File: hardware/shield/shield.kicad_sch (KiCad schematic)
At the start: 15 parts, among them J1 Conn_01x18, J2 Conn_01x20, J3 Conn_01x20, J4 BAT, J5 DCDC, J6 DCDC, U1 NUCLEO-N657X0-Q

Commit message: first schematic version and .ioc pin config
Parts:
- added C10, C11, C12, C14, C15, C16, C17, C18, C19, C20, C21, C22, C23, C24, C25, C28, C29, C6, C7, C8, C9: 0.1uF, Capacitor_SMD:C_0603_1608Metric, symbol Device:C
- added C13: 100uF, Capacitor_Tantalum_SMD:CP_EIA-3528-12_Kemet-T, symbol Device:C_Polarized
- added C26: 1uF, Capacitor_SMD:C_0805_2012Metric, symbol Device:C
- added C27: 47uF, Capacitor_Tantalum_SMD:CP_EIA-3528-12_Kemet-T, symbol Device:C_Polarized
- added J10: Conn_01x09, symbol Connector_Generic:Conn_01x09
- added J11, J12, J24, J25, J27, J28, J29, J30, J31, J7, J8: Conn_01x03, symbol Connector_Generic:Conn_01x03
- added J13, J26, J33: Conn_01x04, symbol Connector_Generic:Conn_01x04
- added J14: DCDC, symbol Connector_Generic:Conn_01x03
- added J15, J16, J17, J18, J19, J20, J21, J22, J23: Conn_01x01_Pin, symbol Connector:Conn_01x01_Pin
- added J32: Conn_01x08, symbol Connector_Generic:Conn_01x08
- added J9: Conn_01x10, symbol Connector_Generic:Conn_01x10
- added R10, R4, R6: 2.2k, symbol Device:R
- added R3, R5: 1.2k, symbol Device:R
- added R7: 10k, symbol Device:R
- added R8: 1k, symbol Device:R
- added R9: 1.5k, symbol Device:R
- added U2: AMS1117-3.3, Package_TO_SOT_SMD:SOT-223-3_TabPin2, symbol Regulator_Linear:AMS1117-3.3
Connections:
- net 3V3: now also C11.1, C15.1, C16.1, C20.1, C21.1, C22.1, C23.1, C26.1, C27.1, C8.1, C9.1, J10.1 (Pin_1), J12.2 (Pin_2), J17.1 (Pin_1), J18.1 (Pin_1), J28.3 (Pin_3), J29.3 (Pin_3), J30.3 (Pin_3), J31.3 (Pin_3), J9.1 (Pin_1), U2.2 (VO); no longer U1.16 (3V3)
- net 5V: now also C10.1, C29.1, J11.2 (Pin_2), J33.4 (Pin_4), U2.3 (VI)
- net 8V: now also C6.1, C7.1, J7.2 (Pin_2), J8.2 (Pin_2)
- net GND: now also C10.2, C11.2, C12.2, C13.2, C14.2, C15.2, C16.2, C17.2, C18.2, C19.2, C20.2, C21.2, C22.2, C23.2, C24.2, C25.2, C26.2, C27.2, C28.2, C29.2, C6.2, C7.2, C8.2, C9.2, J10.2 (Pin_2), J11.1 (Pin_1), J12.1 (Pin_1), J13.1 (Pin_1), J14.3 (Pin_3), J19.1 (Pin_1), J20.1 (Pin_1), J21.1 (Pin_1), J22.1 (Pin_1), J23.1 (Pin_1), J24.1 (Pin_1), J25.1 (Pin_1), J26.1 (Pin_1), J27.1 (Pin_1), J28.1 (Pin_1), J29.1 (Pin_1), J30.1 (Pin_1), J31.1 (Pin_1), J32.1 (Pin_1), J33.1 (Pin_1), J7.1 (Pin_1), J8.1 (Pin_1), J9.2 (Pin_2), R10.2, R4.2, R6.2, R8.1, U2.1 (GND)
- net OV_FLASH: now also U1.64 (PB15); no longer U1.38 (PH2)
- net VCC: now also C24.1, J14.1 (Pin_1), J32.8 (Pin_8), R7.2
- net MOT_PWM1: now reaches U1.40 (NC/PB1)
- net MOT_PWM1: now also J32.7 (Pin_7)
- net IMU_SCK: now reaches U1.42 (PF2)
- net IMU_SCK: now also J9.3 (Pin_3)
- net MOT_BAT: now reaches U1.43 (MOD_PA12)
- net MOT_BAT: now also J32.2 (Pin_2)
- net IR_3: now reaches U1.45 (MOD_PF3)
- net IR_3: now also J30.2 (Pin_2)
- net IR_1: now reaches U1.52 (MOD_PA8)
- net IR_1: now also J28.2 (Pin_2)
- net GEN_TX: now reaches U1.61 (PG3)
- net GEN_TX: now also J24.2 (Pin_2)
- net TEL_TX: now reaches U1.70 (PH3)
- net TEL_TX: now also U1.105 (PD8), J13.2 (Pin_2)
- net TEL_RX: now reaches U1.107 (PD9)
- net TEL_RX: now also J13.3 (Pin_3)
- net BAT_U: now reaches U1.108 (PA1)
- net BAT_U: now also C25.1, R7.1, R8.2
- net UI_SCL: now reaches U1.73 (PH9)
- net UI_SCL: now also J10.7 (Pin_7)
- net UI_SDA: now reaches U1.75 (PC1)
- net UI_SDA: now also J10.8 (Pin_8)
- net SERVO_REAR: now reaches U1.76 (PD6)
- net SERVO_REAR: now also J7.3 (Pin_3)
- net RX_PWM: now reaches U1.83 (PG1)
- net RX_PWM: now also R3.2, R4.1
- net LED_DATA: now reaches U1.85 (PG2)
- net LED_DATA: now also R5.2, R6.1
- net GEN_SCK: now reaches U1.86 (PB9)
- net GEN_SCK: now also J25.3 (Pin_3)
- net GEN_TIM: now reaches U1.93 (PE11)
- net GEN_TIM: now also J26.4 (Pin_4)
- net CMD_RX: now reaches U1.99 (PE0)
- net CMD_RX: now also J12.3 (Pin_3)
- net IMU_MISO: now reaches U1.13 (PC4)
- net IMU_MISO: now also J9.7 (Pin_7)
- net GEN_MOSI: now reaches U1.25 (PC3)
- net GEN_MOSI: now also J25.2 (Pin_2)
- net GEN_RX: now reaches U1.3 (PC2)
- net GEN_RX: now also J24.3 (Pin_3)
- net IR_2: now reaches U1.32 (PF6)
- net IR_2: now also J29.2 (Pin_2)
- net MOT_I: now reaches U1.34 (PA2)
- net MOT_I: now also C28.1, R10.1, R9.2
- net SERVO_FRONT: now reaches U1.36 (PC12)
- net SERVO_FRONT: now also J8.3 (Pin_3)
- net MOT_PWM2: now reaches U1.37 (PC8)
- net MOT_PWM2: now also J32.6 (Pin_6)
- net MOT_STATUS: now reaches U1.110 (PP1)
- net MOT_STATUS: now also J32.4 (Pin_4)
- net MOT_EN: now reaches U1.111 (PP0)
- net MOT_EN: now also J32.5 (Pin_5)
- net UI_BACK: now reaches U1.112 (PP2)
- net UI_BACK: now also J10.3 (Pin_3)
- net UI_A: now reaches U1.114 (PP3)
- net UI_A: now also J10.4 (Pin_4)
- net UI_B: now reaches U1.116 (PP4)
- net UI_B: now also J10.5 (Pin_5)
- net UI_PUSH: now reaches U1.118 (PP5)
- net UI_PUSH: now also J10.6 (Pin_6)
- net UI_CONF: now reaches U1.120 (PP6)
- net UI_CONF: now also J10.9 (Pin_9)
- net GEN_PIN1: now reaches U1.122 (PP7)
- net GEN_PIN1: now also J26.3 (Pin_3)
- net GEN_PIN2: now reaches U1.126 (PP8)
- net GEN_PIN2: now also J26.2 (Pin_2)
- net ENC_A: now reaches U1.127 (PD13)
- net ENC_A: now also J33.2 (Pin_2)
- net IMU_MOSI: now reaches U1.128 (PP9)
- net IMU_MOSI: now also J9.4 (Pin_4)
- net ENC_B: now reaches U1.137 (PG13)
- net ENC_B: now also J33.3 (Pin_3)
- new net: J27.2 (Pin_2), R5.1
- new net: J11.3 (Pin_3), R3.1
- new net: J32.3 (Pin_3), R9.1
- new net 5V_EXT: C12.1, C13.1, C14.1, C17.1, C18.1, C19.1, J13.4 (Pin_4), J14.2 (Pin_2), J15.1 (Pin_1), J16.1 (Pin_1), J27.3 (Pin_3)
- new net IR_4: J31.2 (Pin_2), U1.38 (PH2)
- no-connect marks 23 -> 16
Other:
- note added: "!!!"
- note added: "1V8!!!"
- note added: "Command module"
- note added: "Control"
- note added: "Distance"
- note added: "Extras"
- note added: "Front Servo"
- note added: "IMU"
- note added: "Motor"
- note added: "RC receiver"
- note added: "Rear Servo"
- note added: "Telemetry UART"
- note added: "UI"
- note added: "Using DCDC converter modules like these: https://www.aliexpress.com/item/1005001821783419.html"
- note added: "Using a UI module like this: https://www.hestore.hu/prod_10048024.html#"
- moved on the sheet: C1, C2, C3, C4, C5, F1, J1, J2, J3, J4, J5, J6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

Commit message: minor sch fixes and footprint assignment
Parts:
- removed C1: 220uF, Capacitor_Tantalum_SMD:CP_EIA-3528-12_Kemet-T, symbol Device:C_Polarized
- added C1: 0.1uF, Capacitor_SMD:C_0603_1608Metric, symbol Device:C
- added C30: 1uF, Capacitor_SMD:C_0805_2012Metric, symbol Device:C
- added C31, C32: 220uF, Capacitor_SMD:CP_Elec_6.3x7.7, symbol Device:C_Polarized
- added J34: DCDC, Connector_PinHeader_2.54mm:PinHeader_1x03_P2.54mm_Vertical, symbol Connector_Generic:Conn_01x03
- added J35: Conn_01x03, Connector_PinHeader_1.00mm:PinHeader_1x03_P1.00mm_Vertical, symbol Connector_Generic:Conn_01x03
- added JP1, JP2, JP3: SolderJumper_2_Open, Jumper:SolderJumper-2_P1.3mm_Open_TrianglePad1.0x1.5mm, symbol Jumper:SolderJumper_2_Open
- C13, C2: footprint Capacitor_Tantalum_SMD:CP_EIA-3528-12_Kemet-T -> Capacitor_SMD:CP_Elec_5x5.8
- C27: footprint Capacitor_Tantalum_SMD:CP_EIA-3528-12_Kemet-T -> Capacitor_SMD:CP_Elec_5x5.3
- F1: value 5A -> 8A; footprint Fuse:Fuse_0805_2012Metric -> Fuse:Fuseholder_Blade_Mini_Keystone_3568
- J1: footprint (none) -> Connector_PinHeader_2.00mm:PinHeader_2x09_P2.00mm_Horizontal
- J10: footprint (none) -> Connector_JST:JST_SH_SM09B-SRSS-TB_1x09-1MP_P1.00mm_Horizontal
- J11, J12, J27, J28, J29, J30, J31: footprint (none) -> Connector_JST:JST_SH_SM03B-SRSS-TB_1x03-1MP_P1.00mm_Horizontal
- J13, J33: footprint (none) -> Connector_JST:JST_SH_SM04B-SRSS-TB_1x04-1MP_P1.00mm_Horizontal
- J14, J5, J6: footprint (none) -> Connector_PinHeader_2.54mm:PinHeader_1x03_P2.54mm_Vertical
- J15, J16, J17, J18, J19, J20, J21, J22, J23: footprint (none) -> Connector_Pin:Pin_D0.7mm_L6.5mm_W1.8mm_FlatFork
- J2, J3: footprint (none) -> Connector_PinHeader_2.00mm:PinHeader_2x10_P2.00mm_Horizontal
- J24, J25: footprint (none) -> Connector_PinHeader_1.00mm:PinHeader_1x03_P1.00mm_Vertical
- J26: footprint (none) -> Connector_PinHeader_1.00mm:PinHeader_1x04_P1.00mm_Vertical
- J32: footprint (none) -> Connector_JST:JST_SH_SM08B-SRSS-TB_1x08-1MP_P1.00mm_Horizontal
- J4: footprint (none) -> TerminalBlock:TerminalBlock_MaiXu_MX126-5.0-02P_1x02_P5.00mm
- J7, J8: footprint (none) -> Connector_PinHeader_2.54mm:PinHeader_1x03_P2.54mm_Horizontal
- J9: footprint (none) -> Connector_PinHeader_2.54mm:PinHeader_1x10_P2.54mm_Vertical
- R1, R10, R2, R3, R4, R5, R6, R7, R8, R9: footprint (none) -> Resistor_SMD:R_0603_1608Metric
- U1: footprint FP_NUCLEO-144 - N6 -> hallglib:FP_NUCLEO-144 - N6
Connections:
- net 3V3: now also JP3.1 (A); no longer C20.1, C21.1, C22.1, C23.1, C26.1, C27.1, J28.3 (Pin_3), J29.3 (Pin_3), J30.3 (Pin_3), J31.3 (Pin_3), U2.2 (VO)
- net 5V: now also C30.1, JP1.2 (B); no longer C2.1, C3.1, J5.2 (Pin_2)
- net 5V_EXT: now also C20.1, C21.1, C22.1, C23.1, J28.3 (Pin_3), J29.3 (Pin_3), J30.3 (Pin_3), J31.3 (Pin_3), JP2.2 (B); no longer C12.1, C13.1, J14.2 (Pin_2)
- net GND: now also C1.2, C30.2, C31.2, C32.2, J34.3 (Pin_3), J35.1 (Pin_1)
- net OV_I2C4_SCL: now also J35.2 (Pin_2)
- net OV_I2C4_SDA: now also J35.3 (Pin_3)
- net 8V renamed 8V_1
- net 8V_1: now also C32.1; no longer C7.1, J7.2 (Pin_2)
- net VCC renamed VBAT
- net VBAT: now also J34.1 (Pin_1)
- new net: C12.1, C13.1, J14.2 (Pin_2), JP2.1 (A)
- new net: C2.1, C3.1, J5.2 (Pin_2), JP1.1 (A)
- new net: C26.1, C27.1, JP3.2 (B), U2.2 (VO)
- new net 8V_2: C1.1, C31.1, C7.1, J34.2 (Pin_2), J7.2 (Pin_2)
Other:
- note added: "8V DCDC 1"
- note added: "8V DCDC 2"
- note added: "I2C can be used for something else as well"
- note added: "Polyfuse"
- note removed: "8V DCDC"
- moved on the sheet: C12, C13, C19, C2, C25, C26, C27, C3, C4, C5, C6, F1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

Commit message: larger pin headers
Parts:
- J1: footprint Connector_PinHeader_2.00mm:PinHeader_2x09_P2.00mm_Horizontal -> Connector_PinHeader_2.54mm:PinHeader_2x09_P2.54mm_Horizontal
- J2, J3: footprint Connector_PinHeader_2.00mm:PinHeader_2x10_P2.00mm_Horizontal -> Connector_PinHeader_2.54mm:PinHeader_2x10_P2.54mm_Horizontal
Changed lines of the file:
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@@
 			)
 		)
-		(property "Footprint" "Connector_PinHeader_2.00mm:PinHeader_2x10_P2.00mm_Horizontal"
+		(property "Footprint" "Connector_PinHeader_2.54mm:PinHeader_2x10_P2.54mm_Horizontal"
 			(at 273.05 62.23 0)
 			(effects
@@
 			)
 		)
-		(property "Footprint" "Connector_PinHeader_2.00mm:PinHeader_2x10_P2.00mm_Horizontal"
+		(property "Footprint" "Connector_PinHeader_2.54mm:PinHeader_2x10_P2.54mm_Horizontal"
 			(at 327.66 62.23 0)
 			(effects
@@
 			)
 		)
-		(property "Footprint" "Connector_PinHeader_2.00mm:PinHeader_2x09_P2.00mm_Horizontal"
+		(property "Footprint" "Connector_PinHeader_2.54mm:PinHeader_2x09_P2.54mm_Horizontal"
 			(at 182.88 66.04 0)
 			(effects

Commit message: Approx layout done
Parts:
- J1: value Conn_01x18 -> CAMERA
- J10: value Conn_01x09 -> UI_MODULE
- J11: value Conn_01x03 -> RX_PWM
- J12: value Conn_01x03 -> CMD_RX
- J13: value Conn_01x04 -> TEL_UART
- J14: value DCDC -> 5V_DCDC_2
- J15: value Conn_01x01_Pin -> 5V_TP1
- J16: value Conn_01x01_Pin -> 5V_TP2
- J17: value Conn_01x01_Pin -> 3V3_TP3
- J18: value Conn_01x01_Pin -> 3V3_TP4
- J19: value Conn_01x01_Pin -> GND_TP1
- J2: value Conn_01x20 -> LINE_FRONT
- J20: value Conn_01x01_Pin -> GND_TP2
- J21: value Conn_01x01_Pin -> GND_TP3
- J22: value Conn_01x01_Pin -> GND_TP4
- J23: value Conn_01x01_Pin -> GND
- J24: value Conn_01x03 -> UART
- J25: value Conn_01x03 -> SPI
- J26: value Conn_01x04 -> PINS
- J27: value Conn_01x03 -> LED_DATA
- J28: value Conn_01x03 -> IR_1
- J29: value Conn_01x03 -> IR_2
- J3: value Conn_01x20 -> LINE_BACK
- J30: value Conn_01x03 -> IR_3
- J31: value Conn_01x03 -> IR_4
- J32: value Conn_01x08 -> MOTOR_DRIVER
- J33: value Conn_01x04 -> ENC_AB
- J34: value DCDC -> 8V_DCDC_2
- J35: value Conn_01x03 -> I2C4
- J5: value DCDC -> 5V_DCDC_1
- J6: value DCDC -> 8V_DCDC_1
- J7: value Conn_01x03 -> SERVO_BACK
- J8: value Conn_01x03 -> SERVO_FRONT
- J9: value Conn_01x10 -> IMU
- JP1: value SolderJumper_2_Open -> 5V_1
- JP2: value SolderJumper_2_Open -> 5V_2
- JP3: value SolderJumper_2_Open -> 3V3
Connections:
- net 5V_EXT: now also J27.2 (Pin_2); no longer J27.3 (Pin_3)
- net at R5.1: now also J27.3 (Pin_3); no longer J27.2 (Pin_2)
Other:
- moved on the sheet: R5

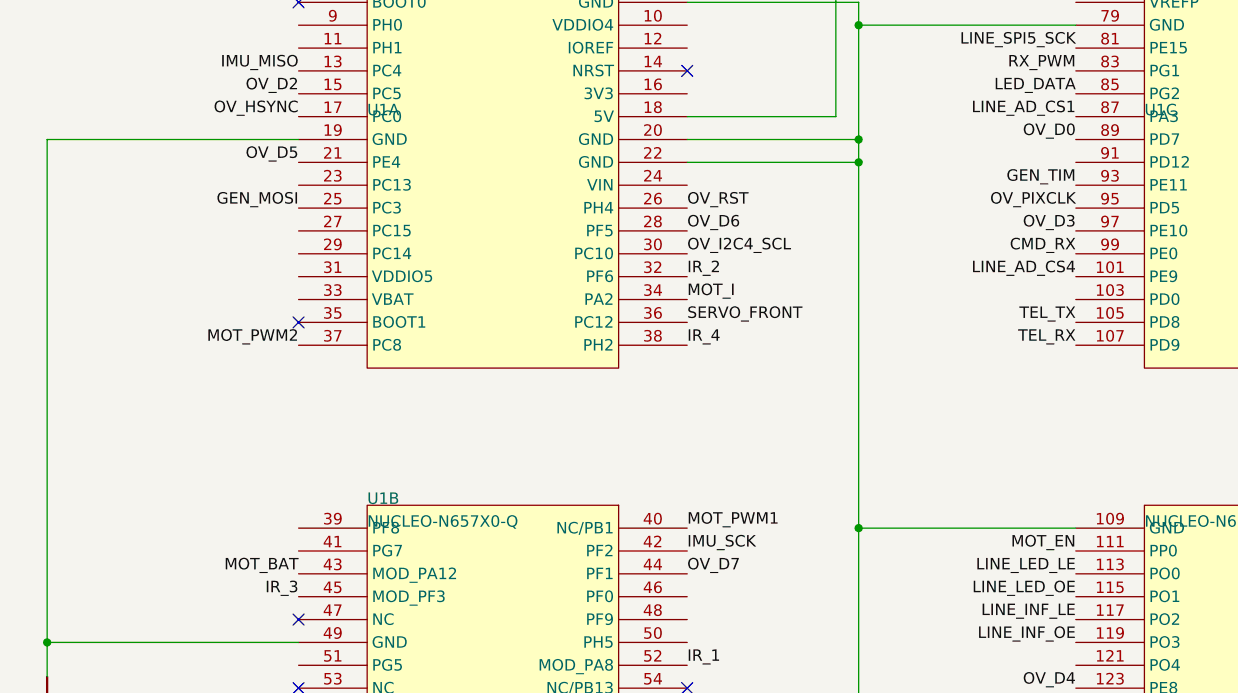
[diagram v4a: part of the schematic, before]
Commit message: servo impl and motor pwm pin changes
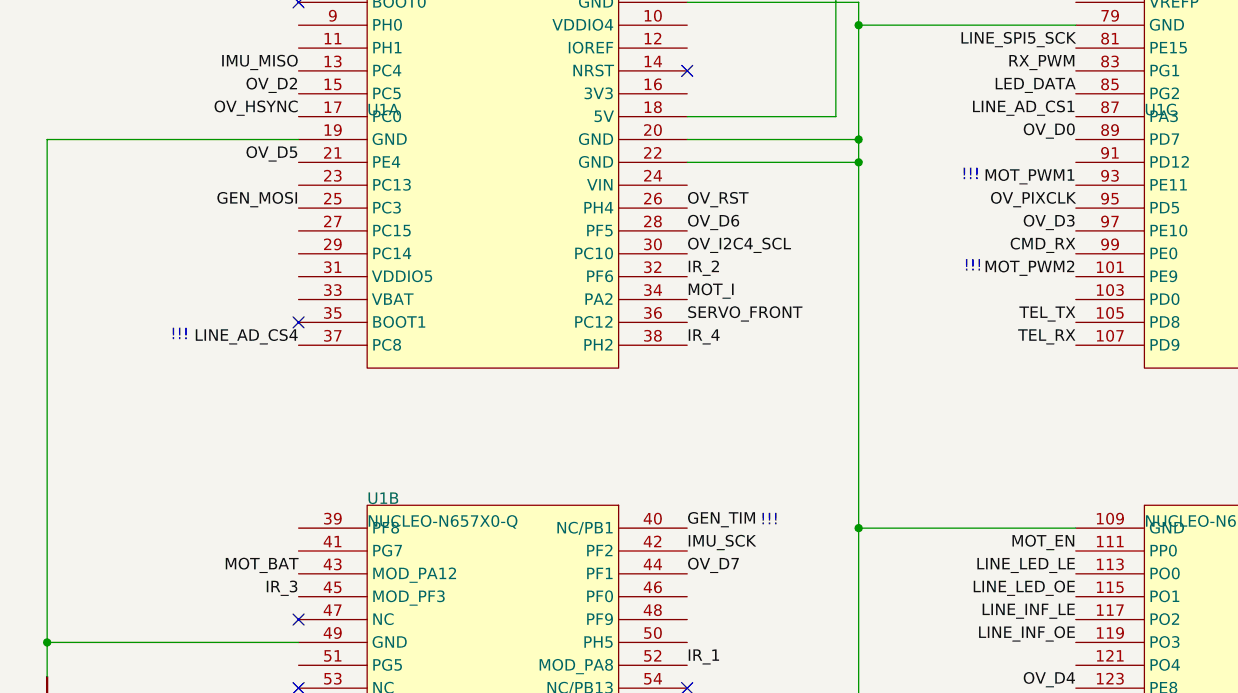
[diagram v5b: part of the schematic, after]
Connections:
- net GEN_TIM: now also U1.40 (NC/PB1); no longer U1.93 (PE11)
- net LINE_AD_CS4: now also U1.37 (PC8); no longer U1.101 (PE9)
- net MOT_PWM1: now also U1.93 (PE11); no longer U1.40 (NC/PB1)
- net MOT_PWM2: now also U1.101 (PE9); no longer U1.37 (PC8)
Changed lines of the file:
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@@
 		)
 	)
+	(text "!!!"
+		(exclude_from_sim no)
+		(at 295.656 264.414 0)
+		(effects
+			(font
+				(size 1.27 1.27)
+				(color 255 0 1 1)
+			)
+		)
+	)
+	(text "!!!"
+		(exclude_from_sim no)
+		(at 273.304 302.768 0)
+		(effects
+			(font
+				(size 1.27 1.27)
+				(color 255 0 1 1)
+			)
+		)
+	)
 	(text "Line sensors"
 		(exclude_from_sim no)
@@
 		)
 	)
+	(text "!!!"
+		(exclude_from_sim no)
+		(at 207.772 282.194 0)
+		(effects
+			(font
+				(size 1.27 1.27)
+				(color 255 0 1 1)
+			)
+		)
+	)
 	(text "Polyfuse"
 		(exclude_from_sim no)
@@
 		)
 	)
+	(text "!!!"
+		(exclude_from_sim no)
+		(at 295.91 274.574 0)
+		(effects
+			(font
+				(size 1.27 1.27)
+				(color 255 0 1 1)
+			)
+		)
+	)
 	(text "Using DCDC converter modules like these:\nhttps://www.aliexpress.com/item/1005001821783419.html"
 		(exclude_from_sim no)
@@
 		)
 	)
-	(label "GEN_TIM"
+	(label "MOT_PWM1"
 		(at 307.34 265.43 180)
 		(effects
@@
 		)
 	)
-	(label "MOT_PWM1"
+	(label "GEN_TIM"
 		(at 264.16 303.53 0)
 		(effects
@@
 		)
 	)
-	(label "MOT_PWM2"
+	(label "LINE_AD_CS4"
 		(at 220.98 283.21 180)
 		(effects
@@
 		)
 	)
-	(label "LINE_AD_CS4"
+	(label "MOT_PWM2"
 		(at 307.34 275.59 180)
 		(effects
